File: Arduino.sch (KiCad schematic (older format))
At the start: 0 parts

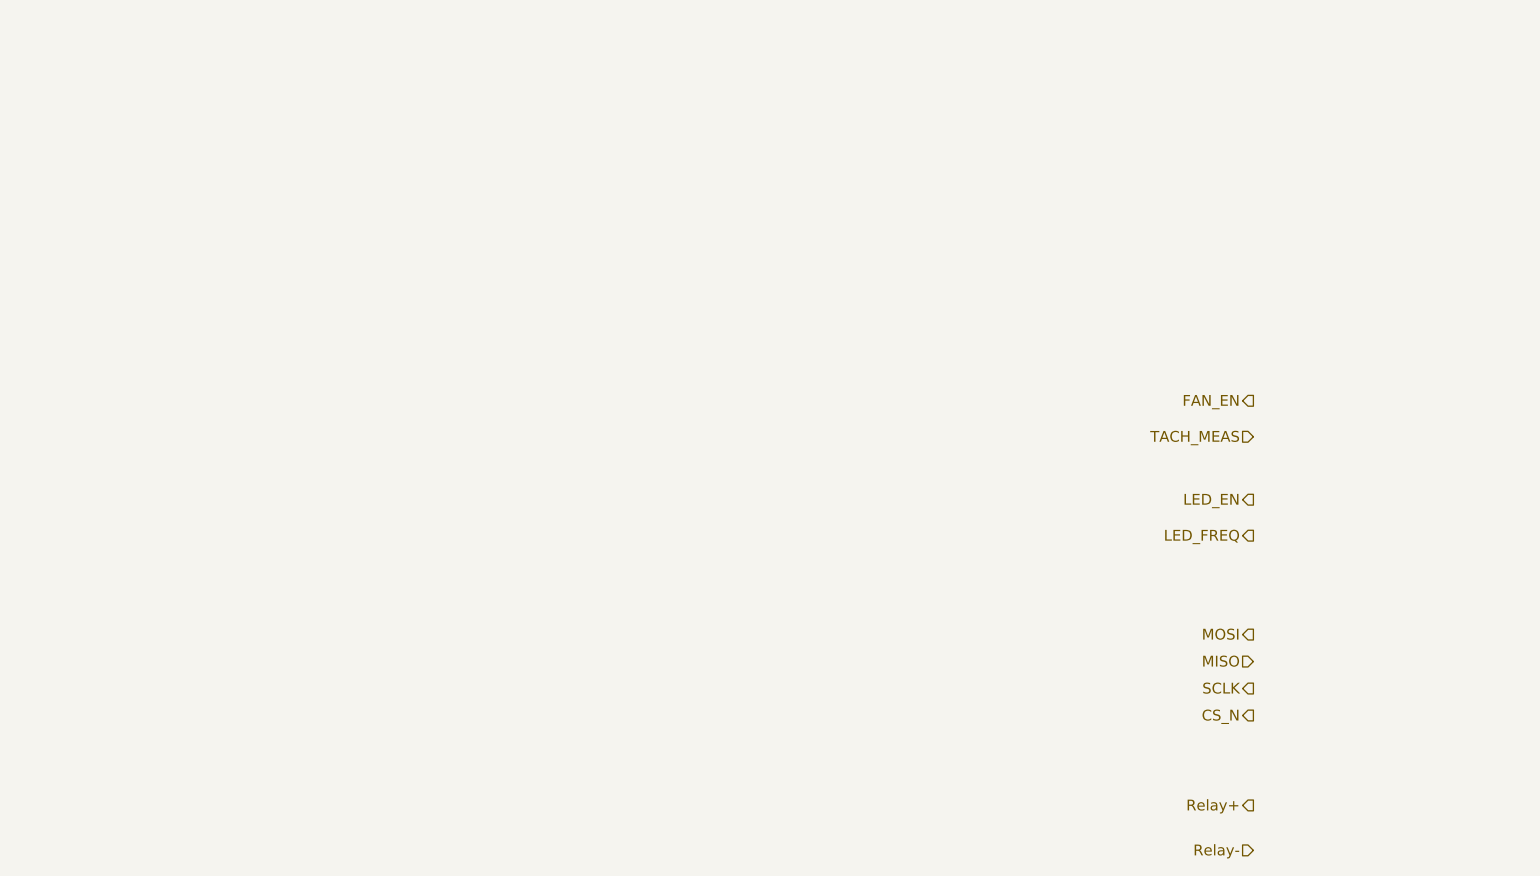
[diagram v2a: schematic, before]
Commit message: 3.9 Understanding The Arduino Module Added content to Arduino and block (header) modules
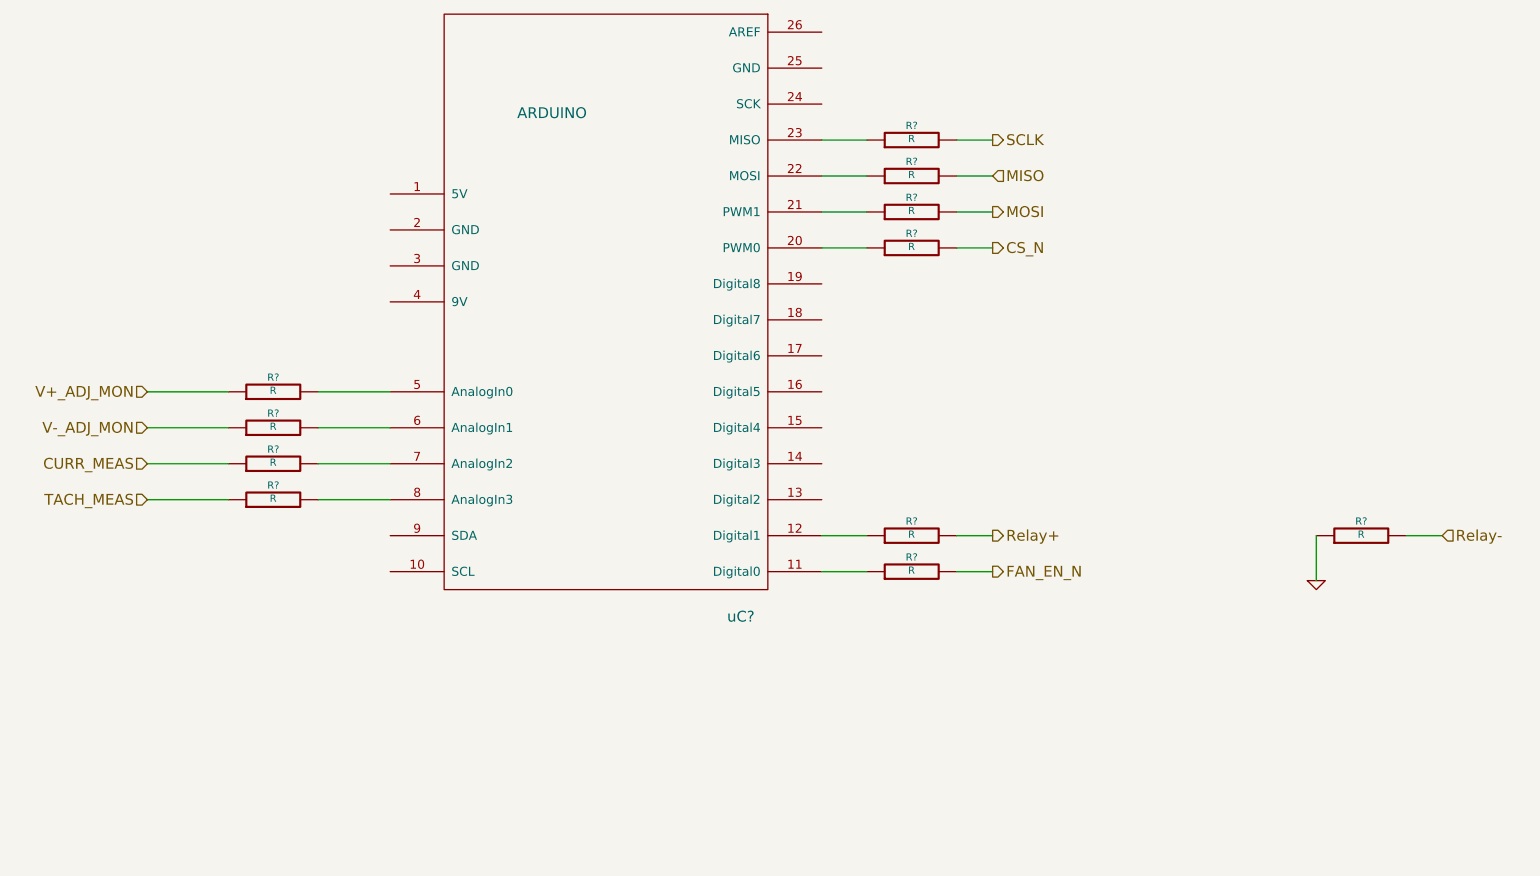
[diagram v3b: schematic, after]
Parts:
- added R? (x11): R, ~, symbol R
- added uC?: ARDUINO, symbol ARDUINO
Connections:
- net CS_N: now also R?.2
- net MISO: now also R?.2
- net MOSI: now also R?.2
- net Relay+: now also R?.2
- net Relay-: now also R?.2
- net SCLK: now also R?.2
- net TACH_MEAS: now also R?.1
- new net: R?.1, uC?.11 (Digital0)
- new net: R?.1, uC?.12 (Digital1)
- new net: R?.1, uC?.20 (PWM0)
- new net: R?.1, uC?.21 (PWM1)
- new net: R?.1, uC?.22 (MOSI)
- new net: R?.1, uC?.23 (MISO)
- new net: R?.2, uC?.5 (AnalogIn0)
- new net: R?.2, uC?.6 (AnalogIn1)
- new net: R?.2, uC?.7 (AnalogIn2)
- new net: R?.2, uC?.8 (AnalogIn3)
- new net CURR_MEAS: R?.1
- new net FAN_EN_N: R?.2
- new net GND: R?.1
- new net V+_ADJ_MON: R?.1
- new net V-_ADJ_MON: R?.1
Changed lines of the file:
@@
 Sheet 2 9
 Title ""
-Date "8 feb 2014"
+Date "10 feb 2014"
 Rev ""
 Comp ""
@@
 Comment4 ""
 $EndDescr
-Text HLabel 7550 6300 0    60   Output ~ 0
+Text HLabel 6100 4800 2    60   Output ~ 0
 Relay+
-Text HLabel 7550 6550 0    60   Input ~ 0
+Text HLabel 6100 3000 2    60   Output ~ 0
+MOSI
+Text HLabel 6100 2800 2    60   Input ~ 0
+MISO
+Text HLabel 6100 2600 2    60   Output ~ 0
+SCLK
+Text HLabel 6100 3200 2    60   Output ~ 0
+CS_N
+Text HLabel 6100 5000 2    60   Output ~ 0
+FAN_EN_N
+Text HLabel 1400 4600 0    60   Input ~ 0
+TACH_MEAS
+$Comp
+L ARDUINO uC?
+U 1 1 52F8F2C5
+P 3950 4900
+F 0 "uC?" H 4700 4550 60  0000 C CNN
+F 1 "ARDUINO" H 3650 7350 60  0000 C CNN
+F 2 "" H 3950 4900 60  0000 C CNN
+F 3 "" H 3950 4900 60  0000 C CNN
+	1    3950 4900
+	1    0    0    -1
+$EndComp
+$Comp
+L R R?
+U 1 1 52F8F2D4
+P 2100 4000
+F 0 "R?" V 2180 4000 40  0000 C CNN
+F 1 "R" V 2107 4001 40  0000 C CNN
+F 2 "~" V 2030 4000 30  0000 C CNN
+F 3 "~" H 2100 4000 30  0000 C CNN
+	1    2100 4000
+	0    -1   -1   0
+$EndComp
+$Comp
+L R R?
+U 1 1 52F8F2E1
+P 2100 4200
+F 0 "R?" V 2180 4200 40  0000 C CNN
+F 1 "R" V 2107 4201 40  0000 C CNN
+F 2 "~" V 2030 4200 30  0000 C CNN
+F 3 "~" H 2100 4200 30  0000 C CNN
+	1    2100 4200
+	0    -1   -1   0
+$EndComp
+$Comp
+L R R?
+U 1 1 52F8F2E7
+P 2100 4400
+F 0 "R?" V 2180 4400 40  0000 C CNN
+F 1 "R" V 2107 4401 40  0000 C CNN
+F 2 "~" V 2030 4400 30  0000 C CNN
+F 3 "~" H 2100 4400 30  0000 C CNN
+	1    2100 4400
+	0    -1   -1   0
+$EndComp
+$Comp
+L R R?
+U 1 1 52F8F2F7
+P 2100 4600
+F 0 "R?" V 2180 4600 40  0000 C CNN
+F 1 "R" V 2107 4601 40  0000 C CNN
+F 2 "~" V 2030 4600 30  0000 C CNN
+F 3 "~" H 2100 4600 30  0000 C CNN
+	1    2100 4600
+	0    -1   -1   0
+$EndComp
+Wire Wire Line
+	2350 4000 2750 4000
+Wire Wire Line
+	2750 4200 2350 4200
+Wire Wire Line
+	2350 4400 2750 4400
+Wire Wire Line
+	2750 4600 2350 4600
+$Comp
+L R R?
+U 1 1 52F8F30B
+P 5650 2600
+F 0 "R?" V 5730 2600 40  0000 C CNN
+F 1 "R" V 5657 2601 40  0000 C CNN
+F 2 "~" V 5580 2600 30  0000 C CNN
+F 3 "~" H 5650 2600 30  0000 C CNN
+	1    5650 2600
+	0    -1   -1   0
+$EndComp
+$Comp
+L R R?
+U 1 1 52F8F318
+P 5650 2800
+F 0 "R?" V 5730 2800 40  0000 C CNN
+F 1 "R" V 5657 2801 40  0000 C CNN
+F 2 "~" V 5580 2800 30  0000 C CNN
+F 3 "~" H 5650 2800 30  0000 C CNN
+	1    5650 2800
+	0    -1   -1   0
+$EndComp
+$Comp
+L R R?
+U 1 1 52F8F31E
+P 5650 3000
+F 0 "R?" V 5730 3000 40  0000 C CNN
+F 1 "R" V 5657 3001 40  0000 C CNN
+F 2 "~" V 5580 3000 30  0000 C CNN
+F 3 "~" H 5650 3000 30  0000 C CNN
+	1    5650 3000
+	0    -1   -1   0
+$EndComp
+$Comp
+L R R?
+U 1 1 52F8F324
+P 5650 3200
+F 0 "R?" V 5730 3200 40  0000 C CNN
+F 1 "R" V 5657 3201 40  0000 C CNN
+F 2 "~" V 5580 3200 30  0000 C CNN
+F 3 "~" H 5650 3200 30  0000 C CNN
+	1    5650 3200
+	0    -1   -1   0
+$EndComp
+$Comp
+L R R?
+U 1 1 52F8F32A
+P 5650 4800
+F 0 "R?" V 5730 4800 40  0000 C CNN
+F 1 "R" V 5657 4801 40  0000 C CNN
+F 2 "~" V 5580 4800 30  0000 C CNN
+F 3 "~" H 5650 4800 30  0000 C CNN
+	1    5650 4800
+	0    -1   -1   0
+$EndComp
+$Comp
+L R R?
+U 1 1 52F8F330
+P 5650 5000
+F 0 "R?" V 5730 5000 40  0000 C CNN
+F 1 "R" V 5657 5001 40  0000 C CNN
+F 2 "~" V 5580 5000 30  0000 C CNN
+F 3 "~" H 5650 5000 30  0000 C CNN
+	1    5650 5000
+	0    -1   -1   0
+$EndComp
+Text HLabel 8600 4800 2    60   Input ~ 0
 Relay-
-Text HLabel 7550 5350 0    60   Output ~ 0
-MOSI
-Text HLabel 7550 5500 0    60   Input ~ 0
-MISO
-Text HLabel 7550 5650 0    60   Output ~ 0
-SCLK
-Text HLabel 7550 5800 0    60   Output ~ 0
-CS_N
-Text HLabel 7550 4600 0    60   Output ~ 0
-LED_EN
-Text HLabel 7550 4800 0    60   Output ~ 0
-LED_FREQ
-Text HLabel 7550 4050 0    60   Output ~ 0
-FAN_EN
-Text HLabel 7550 4250 0    60   Input ~ 0
-TACH_MEAS
+$Comp
+L GND #PWR?
+U 1 1 52F8F33B
+P 7900 5050
+F 0 "#PWR?" H 7900 5050 30  0001 C CNN
+F 1 "GND" H 7900 4980 30  0001 C CNN
+F 2 "" H 7900 5050 60  0000 C CNN
+F 3 "" H 7900 5050 60  0000 C CNN
+	1    7900 5050
+	1    0    0    -1
+$EndComp
+$Comp
+L R R?
+U 1 1 52F8F34C
+P 8150 4800
+F 0 "R?" V 8230 4800 40  0000 C CNN
+F 1 "R" V 8157 4801 40  0000 C CNN
+F 2 "~" V 8080 4800 30  0000 C CNN
+F 3 "~" H 8150 4800 30  0000 C CNN
+	1    8150 4800
+	0    -1   -1   0
+$EndComp
+Wire Wire Line
+	8600 4800 8400 4800
+Wire Wire Line
+	7900 4800 7900 5050
+Text HLabel 1400 4000 0    60   Input ~ 0
+V+_ADJ_MON
+Text HLabel 1400 4200 0    60   Input ~ 0
+V-_ADJ_MON
+Text HLabel 1400 4400 0    60   Input ~ 0
+CURR_MEAS
+Wire Wire Line
+	1400 4000 1850 4000
+Wire Wire Line
+	1400 4200 1850 4200
+Wire Wire Line
+	1850 4400 1400 4400
+Wire Wire Line
+	1400 4600 1850 4600
+Wire Wire Line
+	5150 2600 5400 2600
+Wire Wire Line
+	5400 2800 5150 2800
+Wire Wire Line
+	5150 3000 5400 3000
+Wire Wire Line
+	5400 3200 5150 3200
+Wire Wire Line
+	5900 2600 6100 2600
+Wire Wire Line
+	5900 2800 6100 2800
+Wire Wire Line
+	5900 3000 6100 3000
+Wire Wire Line
+	5900 3200 6100 3200
+Wire Wire Line
+	5150 4800 5400 4800
+Wire Wire Line
+	5400 5000 5150 5000
+Wire Wire Line
+	5900 4800 6100 4800
+Wire Wire Line
+	5900 5000 6100 5000
 $EndSCHEMATC

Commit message: 3.10   Revisiting The Current/Fan Module End of Module 3, lots of cleanup/changes all over the place.
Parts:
- removed uC?: ARDUINO, symbol ARDUINO
- added R? (x4): R, ~, symbol R
- added uC?: ARDUINO, ~, symbol ARDUINO
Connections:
- net at R?.1: now also uC?.20 (PWM0)
- net at R?.1: now also uC?.12 (Digital1)
- net at R?.1: now also uC?.18 (Digital7)
- net at R?.1: now also uC?.21 (PWM1)
- net at R?.1: now also uC?.22 (MOSI)
- net at R?.1: now also uC?.23 (MISO)
- net at R?.2: now also uC?.5 (AnalogIn0)
- net at R?.2: now also uC?.6 (AnalogIn1)
- net at R?.2: now also uC?.7 (AnalogIn2)
- net at R?.2: now also uC?.8 (AnalogIn3)
- net CS_N renamed ADC_CS_N
- net FAN_EN_N renamed FAN_PWM
- new net: R?.1, uC?.17 (Digital6)
- new net: R?.1, uC?.19 (Digital8)
- new net: R?.1, uC?.11 (Digital0)
- new net: R?.2, uC?.4 (9V)
- new net +12P: R?.1
- new net DAC_CS_N: R?.2
- new net FAN_MODE: R?.2
- new net LED_EN_PWM: R?.2
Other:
- moved on the sheet: R?
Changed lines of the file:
@@
 $Descr A4 11693 8268
 encoding utf-8
-Sheet 2 9
+Sheet 9 9
 Title ""
 Date "10 feb 2014"
@@
 Text HLabel 6100 2600 2    60   Output ~ 0
 SCLK
+Text HLabel 6100 3600 2    60   Output ~ 0
+ADC_CS_N
 Text HLabel 6100 3200 2    60   Output ~ 0
-CS_N
-Text HLabel 6100 5000 2    60   Output ~ 0
-FAN_EN_N
+FAN_PWM
 Text HLabel 1400 4600 0    60   Input ~ 0
 TACH_MEAS
-$Comp
-L ARDUINO uC?
-U 1 1 52F8F2C5
-P 3950 4900
-F 0 "uC?" H 4700 4550 60  0000 C CNN
-F 1 "ARDUINO" H 3650 7350 60  0000 C CNN
-F 2 "" H 3950 4900 60  0000 C CNN
-F 3 "" H 3950 4900 60  0000 C CNN
-	1    3950 4900
-	1    0    0    -1
-$EndComp
 $Comp
 L R R?
@@
 L R R?
 U 1 1 52F8F324
-P 5650 3200
-F 0 "R?" V 5730 3200 40  0000 C CNN
-F 1 "R" V 5657 3201 40  0000 C CNN
-F 2 "~" V 5580 3200 30  0000 C CNN
-F 3 "~" H 5650 3200 30  0000 C CNN
-	1    5650 3200
+P 5650 3600
+F 0 "R?" V 5730 3600 40  0000 C CNN
+F 1 "R" V 5657 3601 40  0000 C CNN
+F 2 "~" V 5580 3600 30  0000 C CNN
+F 3 "~" H 5650 3600 30  0000 C CNN
+	1    5650 3600
 	0    -1   -1   0
 $EndComp
@@
 L R R?
 U 1 1 52F8F330
-P 5650 5000
-F 0 "R?" V 5730 5000 40  0000 C CNN
-F 1 "R" V 5657 5001 40  0000 C CNN
-F 2 "~" V 5580 5000 30  0000 C CNN
-F 3 "~" H 5650 5000 30  0000 C CNN
-	1    5650 5000
+P 5650 3200
+F 0 "R?" V 5730 3200 40  0000 C CNN
+F 1 "R" V 5657 3201 40  0000 C CNN
+F 2 "~" V 5580 3200 30  0000 C CNN
+F 3 "~" H 5650 3200 30  0000 C CNN
+	1    5650 3200
 	0    -1   -1   0
 $EndComp
@@
 	5150 3000 5400 3000
 Wire Wire Line
+	5400 3600 5150 3600
+Wire Wire Line
+	5900 2600 6100 2600
+Wire Wire Line
+	5900 2800 6100 2800
+Wire Wire Line
+	5900 3000 6100 3000
+Wire Wire Line
+	5900 3600 6100 3600
+Wire Wire Line
+	5150 4800 5400 4800
+Wire Wire Line
 	5400 3200 5150 3200
 Wire Wire Line
-	5900 2600 6100 2600
-Wire Wire Line
-	5900 2800 6100 2800
-Wire Wire Line
-	5900 3000 6100 3000
+	5900 4800 6100 4800
 Wire Wire Line
 	5900 3200 6100 3200
-Wire Wire Line
-	5150 4800 5400 4800
-Wire Wire Line
-	5400 5000 5150 5000
-Wire Wire Line
-	5900 4800 6100 4800
+Text HLabel 6100 3800 2    60   Output ~ 0
+DAC_CS_N
+$Comp
+L R R?
+U 1 1 52F844DD
+P 5650 3800
+F 0 "R?" V 5730 3800 40  0000 C CNN
+F 1 "R" V 5657 3801 40  0000 C CNN
+F 2 "~" V 5580 3800 30  0000 C CNN
+F 3 "~" H 5650 3800 30  0000 C CNN
+	1    5650 3800
+	0    -1   -1   0
+$EndComp
+Wire Wire Line
+	5400 3800 5150 3800
+Wire Wire Line
+	5900 3800 6100 3800
+Text HLabel 6100 3400 2    60   Output ~ 0
+LED_EN_PWM
+$Comp
+L R R?
+U 1 1 52F844E8
+P 5650 3400
+F 0 "R?" V 5730 3400 40  0000 C CNN
+F 1 "R" V 5657 3401 40  0000 C CNN
+F 2 "~" V 5580 3400 30  0000 C CNN
+F 3 "~" H 5650 3400 30  0000 C CNN
+	1    5650 3400
+	0    -1   -1   0
+$EndComp
+Wire Wire Line
+	5400 3400 5150 3400
+Wire Wire Line
+	5900 3400 6100 3400
+$Comp
+L ARDUINO uC?
+U 1 1 52F847B6
+P 3950 4900
+F 0 "uC?" H 4700 4550 60  0000 C CNN
+F 1 "ARDUINO" H 3650 7350 60  0000 C CNN
+F 2 "~" H 3950 4900 60  0000 C CNN
+F 3 "~" H 3950 4900 60  0000 C CNN
+	1    3950 4900
+	1    0    0    -1
+$EndComp
+Text HLabel 6100 5000 2    60   Output ~ 0
+FAN_MODE
+$Comp
+L R R?
+U 1 1 52F897E0
+P 5650 5000
+F 0 "R?" V 5730 5000 40  0000 C CNN
+F 1 "R" V 5657 5001 40  0000 C CNN
+F 2 "~" V 5580 5000 30  0000 C CNN
+F 3 "~" H 5650 5000 30  0000 C CNN
+	1    5650 5000
+	0    -1   -1   0
+$EndComp
+Wire Wire Line
+	5150 5000 5400 5000
 Wire Wire Line
 	5900 5000 6100 5000
+$Comp
+L R R?
+U 1 1 52F897E9
+P 2100 3500
+F 0 "R?" V 2180 3500 40  0000 C CNN
+F 1 "R" V 2107 3501 40  0000 C CNN
+F 2 "~" V 2030 3500 30  0000 C CNN
+F 3 "~" H 2100 3500 30  0000 C CNN
+	1    2100 3500
+	0    -1   -1   0
+$EndComp
+Wire Wire Line
+	2750 3500 2350 3500
+$Comp
+L +12P #PWR?
+U 1 1 52F8980E
+P 1600 3200
+F 0 "#PWR?" H 1600 3170 30  0001 C CNN
+F 1 "+12P" H 1600 3300 30  0000 C CNN
+F 2 "" H 1600 3200 60  0000 C CNN
+F 3 "" H 1600 3200 60  0000 C CNN
+	1    1600 3200
+	1    0    0    -1
+$EndComp
+Wire Wire Line
+	1850 3500 1600 3500
+Wire Wire Line
+	1600 3500 1600 3200
 $EndSCHEMATC

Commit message: replaced faulty arduino part with updated library
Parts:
- removed uC?: ARDUINO, ~, symbol ARDUINO
- added uC?: ARDUINO, ~, symbol ARDUINO
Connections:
- net at R?.1: now also uC?.17 (Digital6)
- net at R?.1: now also uC?.19 (Digital8)
- net at R?.1: now also uC?.11 (Digital0)
- net at R?.1: now also uC?.12 (Digital1)
- net at R?.1: now also uC?.18 (Digital7)
- net at R?.1: now also uC?.20 (PWM0)
- net at R?.1: now also uC?.21 (PWM1)
- net at R?.1: now also uC?.22 (MOSI)
- net at R?.1: now also uC?.23 (MISO)
- net at R?.2: now also uC?.4 (9V)
- net at R?.2: now also uC?.5 (AnalogIn0)
- net at R?.2: now also uC?.6 (AnalogIn1)
- net at R?.2: now also uC?.7 (AnalogIn2)
- net at R?.2: now also uC?.8 (AnalogIn3)
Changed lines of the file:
@@
 Sheet 9 9
 Title ""
-Date "10 feb 2014"
+Date "13 feb 2014"
 Rev ""
 Comp ""
@@
 Wire Wire Line
 	5900 3400 6100 3400
-$Comp
-L ARDUINO uC?
-U 1 1 52F847B6
-P 3950 4900
-F 0 "uC?" H 4700 4550 60  0000 C CNN
-F 1 "ARDUINO" H 3650 7350 60  0000 C CNN
-F 2 "~" H 3950 4900 60  0000 C CNN
-F 3 "~" H 3950 4900 60  0000 C CNN
-	1    3950 4900
-	1    0    0    -1
-$EndComp
 Text HLabel 6100 5000 2    60   Output ~ 0
 FAN_MODE
@@
 Wire Wire Line
 	1600 3500 1600 3200
+$Comp
+L ARDUINO uC?
+U 1 1 52FCA476
+P 3950 4900
+F 0 "uC?" H 4700 4550 60  0000 C CNN
+F 1 "ARDUINO" H 3650 7350 60  0000 C CNN
+F 2 "~" H 3950 4900 60  0000 C CNN
+F 3 "~" H 3950 4900 60  0000 C CNN
+	1    3950 4900
+	1    0    0    -1
+$EndComp
 $EndSCHEMATC
